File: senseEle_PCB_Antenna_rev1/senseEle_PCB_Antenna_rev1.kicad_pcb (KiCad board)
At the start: 2 copper layers, 76 x 45 mm, 53 parts, among them J2 Conn_02x03_Odd_Even, Q1 IRLML6401, U1 KX003-1077, U2 MIC5504-1.8YM5, U3 MDBT42Q, U4 CC1175, U6 SI7201-B-00-FV, X1 TXKTPCSANF-32, Y1 Crystal

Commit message: routing done.
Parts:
- moved MK2 27.0 mm to (56.0, 13.0)
- moved MK4 27.0 mm to (56.0, 52.0)
- moved C9 7.83 mm to (31.5, 50.0), turned to 90 degrees
- moved C20 4.88 mm to (33.0, 47.7)
- moved Q1 4.88 mm to (34.5, 50.0)
- moved C21 3.99 mm to (33.0, 44.8)
- moved Y1 3.54 mm to (30.0, 46.2)
- moved BT1 3.32 mm to (40.0, 50.0)
- moved C7 1.50 mm to (35.8, 32.2)
- moved C19 0.97 mm to (26.2, 50.5)
- moved C18 0.64 mm to (24.8, 50.5)
- moved L11 0.54 mm to (22.8, 50.5), turned to 90 degrees
- moved C17 0.43 mm to (19.1, 50.5), turned to 270 degrees
- moved L10 0.35 mm to (20.8, 50.5), turned to 270 degrees
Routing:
- net GND: track 5.71 -> 86.6 mm, vias 0 -> 30
- net VDD_CC112x: track 50.6 -> 111.3 mm, vias 0 -> 3
- net VDD: track 30.1 -> 84.2 mm, vias 1 -> 3
- net /CC1120/GPIO2: track 0.00 -> 21.6 mm
- net /CC1120/GPIO3: track 0.00 -> 21.4 mm
- net /CC1120/RESET_N: track 0.00 -> 21.2 mm
- net /CC1120/CSN: track 0.00 -> 20.9 mm
- net /CC1120/GPIO0: track 0.00 -> 19.7 mm
- net /CC1120/MISO: track 0.00 -> 18.8 mm
- net /CC1120/SCLK: track 0.00 -> 18.0 mm
- net /CC1120/MOSI: track 0.00 -> 18.0 mm
- net /nRF_Module/XL1: track 0.00 -> 8.35 mm
- net /nRF_Module/XL2: track 0.00 -> 8.31 mm
- net /nRF_Module/DEC4: track 0.00 -> 5.07 mm
- net Net-(BT1-Pad1): track 0.00 -> 4.50 mm
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
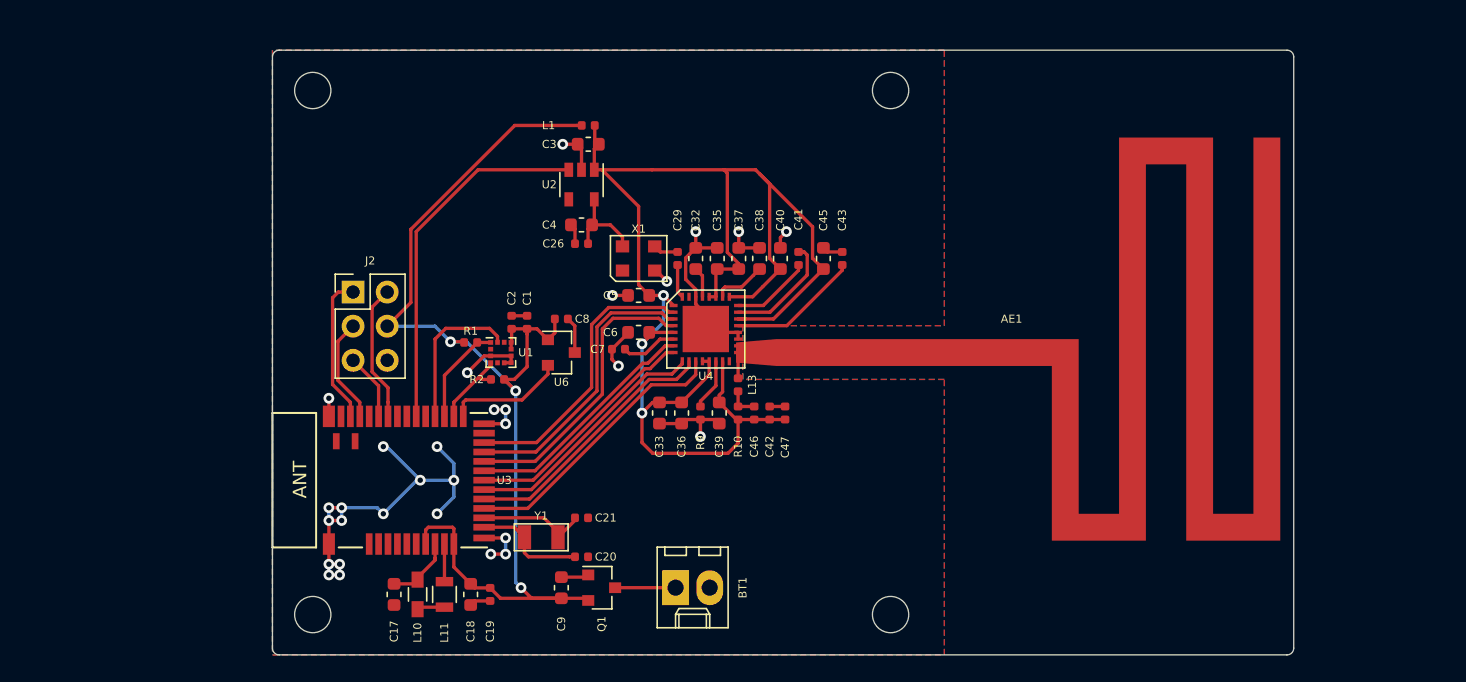
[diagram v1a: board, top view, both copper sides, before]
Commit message: Update SenseEle PCB antenna design with tapered antenna
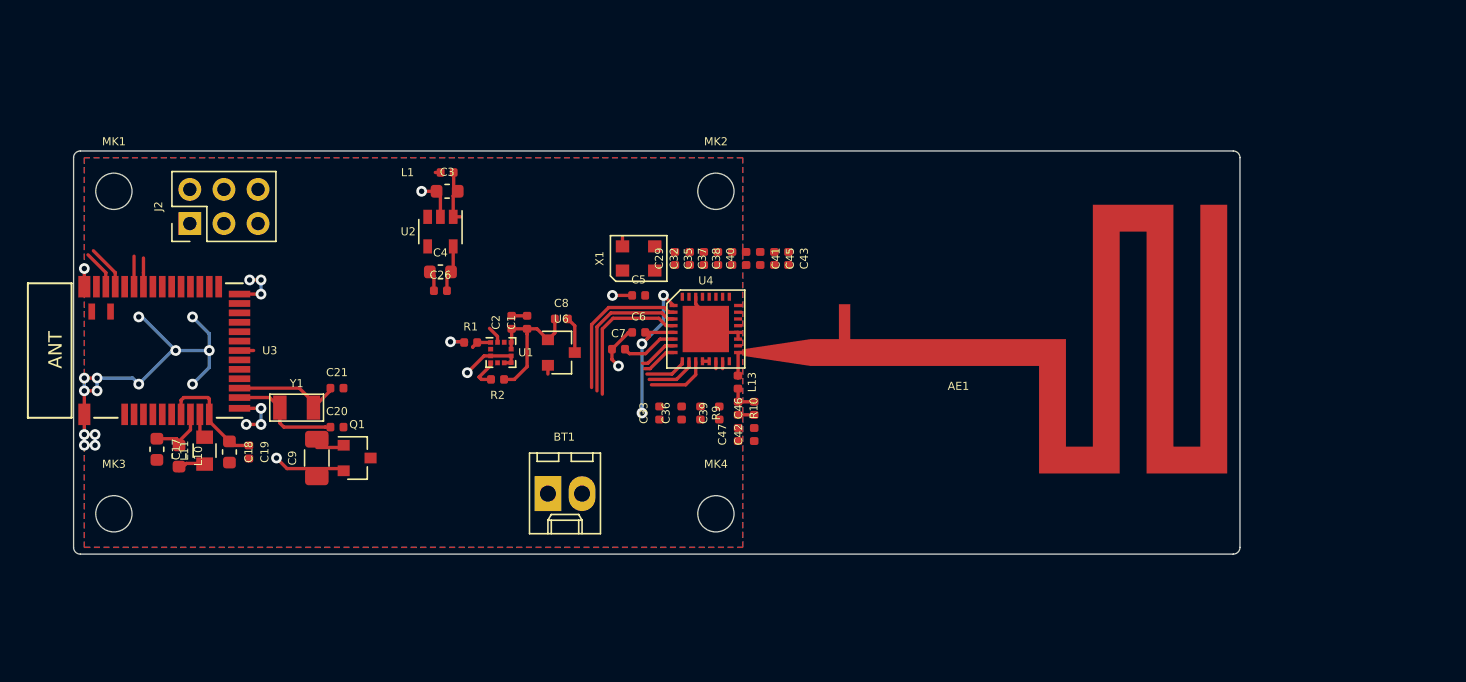
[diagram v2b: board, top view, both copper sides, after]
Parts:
- AE1: footprint sense:dn024_pa_match -> sense_fp:DN024_taper
- BT1: footprint sense:Molex_KK-6410-02_02x2.54mm_Straight -> sense_fp:Molex_KK-6410-02_02x2.54mm_Straight
- C1, C19, C2, C20, C21, C26, C29, C41, C42, C43, C46, C47, C7, C8: footprint sense:C_0402_1005Metric -> sense_fp:C_0402_1005Metric
- C17, C18, C3, C4: footprint sense:C_0603_1608Metric -> sense_fp:C_0603_1608Metric
- C32, C33, C35, C36, C37, C38, C39, C40, C45, C5, C6: footprint sense:C_0603_1608Metric -> sense_fp:C_0402_1005Metric
- C9: footprint sense:C_0603_1608Metric -> sense_fp:C_1206_3216Metric
- L10: footprint sense:L_0603_HandSoldering -> sense_fp:C_0603_1608Metric
- L11: footprint sense:L_0805 -> sense_fp:C_0805
- MK1, MK2, MK3, MK4: footprint sense:MountingHole_2.7mm_M2.5 -> sense_fp:MountingHole_2.7mm_M2.5
- Q1, U6: footprint sense:SOT-23 -> sense_fp:SOT-23
- R1, R10, R2, R9: footprint Resistor_SMD:R_0402_1005Metric -> sense_fp:C_0402_1005Metric
- U3: footprint sense:mdbt42Q -> sense_fp:mdbt42Q
- U4: footprint sense:CC1120 -> sense_fp:CC1120
- X1: footprint sense:TXKTPCSANF-32 -> sense_fp:TXKTPCSANF-32
- Y1: footprint sense:Q13FC1350000400_SMD Crystals 32.768KHz -> sense_fp:Q13FC1350000400_SMD Crystals 32.768KHz
- moved C18 20.8 mm to (6.80, 39.9)
- moved C19 20.8 mm to (8.25, 39.9)
- moved L11 20.8 mm to (4.95, 39.8)
- moved C17 20.7 mm to (1.40, 39.7)
- moved C20 20.6 mm to (14.8, 38.0)
- moved C21 20.6 mm to (14.8, 35.1)
- moved C9 20.6 mm to (13.3, 40.4)
- moved Q1 20.6 mm to (16.3, 40.4)
- moved U3 20.6 mm to (1.30, 32.4)
- moved Y1 20.6 mm to (11.8, 36.6)
- moved L10 20.5 mm to (3.05, 40.2)
- moved MK1 16.6 mm to (-1.80, 20.5)
- moved MK3 16.6 mm to (-1.80, 44.5)
- moved MK2 15.0 mm to (43.0, 20.5)
- moved MK4 15.0 mm to (43.0, 44.5)
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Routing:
- net VDD_CC112x: track 111.3 -> 19.9 mm
- net VDD: track 84.2 -> 27.9 mm, vias 3 -> 2
- net /CC1120/TCXO_EN: track 27.0 -> 0.00 mm
- net GND: track 86.6 -> 63.9 mm, vias 30 -> 25
- net /CC1120/CSN: track 20.9 -> 4.61 mm
- net /CC1120/GPIO0: track 19.7 -> 3.77 mm
- net /CC1120/MISO: track 18.8 -> 3.13 mm
- net /CC1120/MOSI: track 18.0 -> 2.85 mm
- net /CC1120/SCLK: track 18.0 -> 3.69 mm
- net /CC1120/GPIO2: track 21.6 -> 10.7 mm
- net Net-(AE1-Pad1): track 15.3 -> 4.87 mm
- net /CC1120/GPIO3: track 21.4 -> 11.1 mm
- net /nRF_Module/INT: track 11.4 -> 1.29 mm
- net Net-(C43-Pad2): track 9.85 -> 0.00 mm
- net /CC1120/RESET_N: track 21.2 -> 11.5 mm
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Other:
- board size 76 x 45 mm -> 86.8 x 30 mm

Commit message: senseEle_PCB_Antenna_rev1 Gerber files ready.
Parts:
- moved C26 21.9 mm to (43.0, 20.2)
- moved C4 21.9 mm to (43.0, 18.9)
- moved U2 21.8 mm to (43.0, 16.0)
- moved C3 21.3 mm to (43.0, 13.2)
- moved L1 21.3 mm to (43.0, 11.8)
- moved U6 20.1 mm to (35.0, 12.8), turned to 270 degrees
- moved C8 18.3 mm to (37.5, 12.8), turned to 270 degrees
- moved Y1 17.7 mm to (27.5, 28.4)
- moved C2 17.6 mm to (44.6, 25.0), turned to 270 degrees
- moved C21 17.2 mm to (30.6, 28.4)
- moved L10 17.2 mm to (18.6, 33.0)
- moved C6 17.1 mm to (51.1, 20.9), turned to 270 degrees
- moved C18 17.0 mm to (22.4, 33.0)
- moved C19 17.0 mm to (23.8, 33.0)
- moved C7 17.0 mm to (50.6, 24.0)
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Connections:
- U3 pad 25: /nRF_Module/HallEffect -> /nRF_Module/SDA
- U3 pad 26: /nRF_Module/SDA -> /nRF_Module/SCL
- U3 pad 27: /nRF_Module/SCL -> /nRF_Module/INT
- U3 pad 28: /nRF_Module/INT -> /CC1120/TCXO_EN
- U3 pad 30: /CC1120/TCXO_EN -> /nRF_Module/HallEffect
- U3 pad 33: /nRF_Module/RX -> Net-(U3-Pad33)
- U3 pad 38: Net-(U3-Pad38) -> /nRF_Module/RX
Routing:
- net VDD: track 27.9 -> 113.2 mm, vias 2 -> 4
- net VDD_CC112x: track 19.9 -> 77.3 mm, vias 3 -> 6
- net GND: track 63.9 -> 99.7 mm, vias 25 -> 27
- net /CC1120/GPIO0: track 3.77 -> 37.3 mm
- net /CC1120/CSN: track 4.61 -> 37.8 mm
- net /CC1120/MOSI: track 2.85 -> 35.9 mm
- net /CC1120/MISO: track 3.13 -> 36.2 mm
- net /CC1120/SCLK: track 3.69 -> 35.8 mm
- net /CC1120/GPIO2: track 10.7 -> 37.6 mm
- net /CC1120/GPIO3: track 11.1 -> 37.8 mm
- net /CC1120/TCXO_EN: track 0.00 -> 26.5 mm
- net /CC1120/RESET_N: track 11.5 -> 38.0 mm
- net /nRF_Module/INT: track 1.29 -> 26.5 mm
- net /nRF_Module/SCL: track 1.49 -> 24.2 mm
- net /nRF_Module/SDA: track 2.41 -> 24.5 mm
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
